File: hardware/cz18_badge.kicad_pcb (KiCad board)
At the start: 2 copper layers, 91.5 x 99.6 mm, 37 parts, among them J1 Dev breakout (opt.), J2 VCC (max 5V), J3 GND, J4 LEDS OUT, SW1 MODE, SW2 SLOT, SW3 LEARN, SW4 PLAY, U1 CHQ1838, U2 NRF24L01 (opt.)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

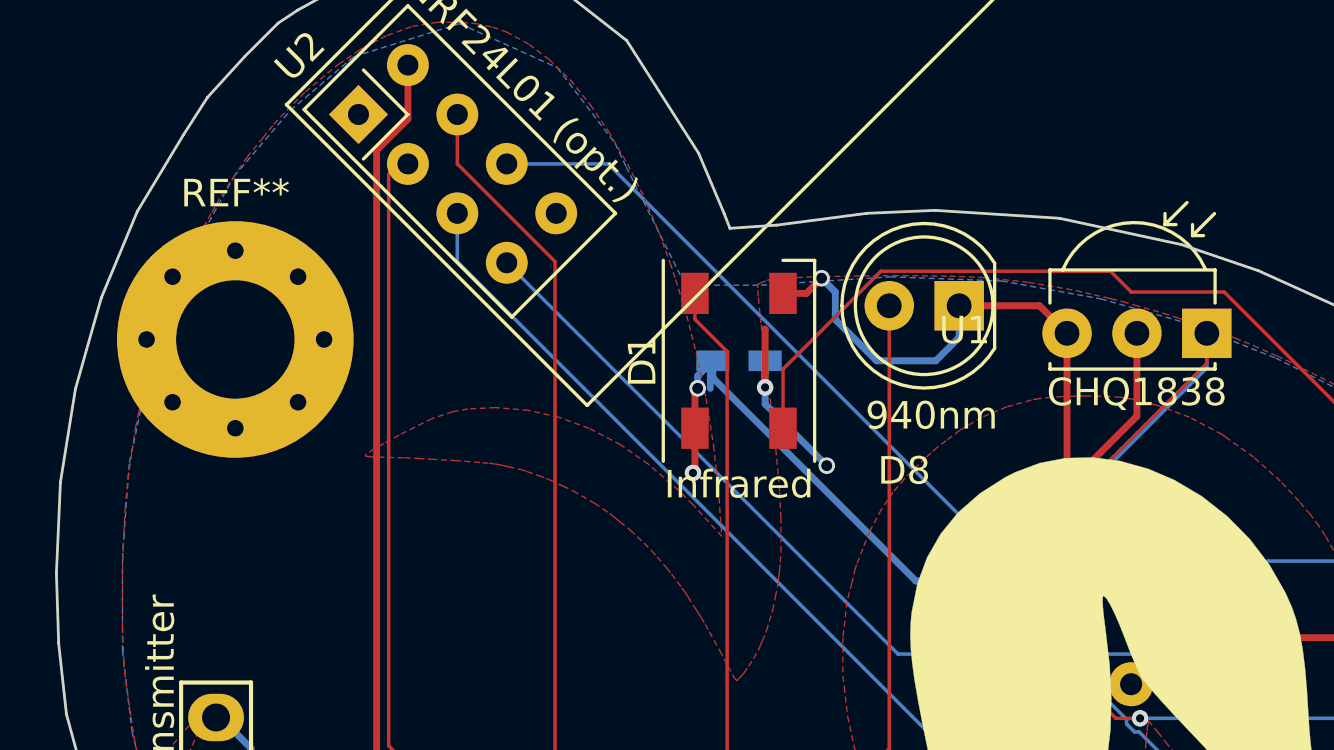
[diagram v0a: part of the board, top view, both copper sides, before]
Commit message: Fixed IR receiver pinout not matching CHQ1838
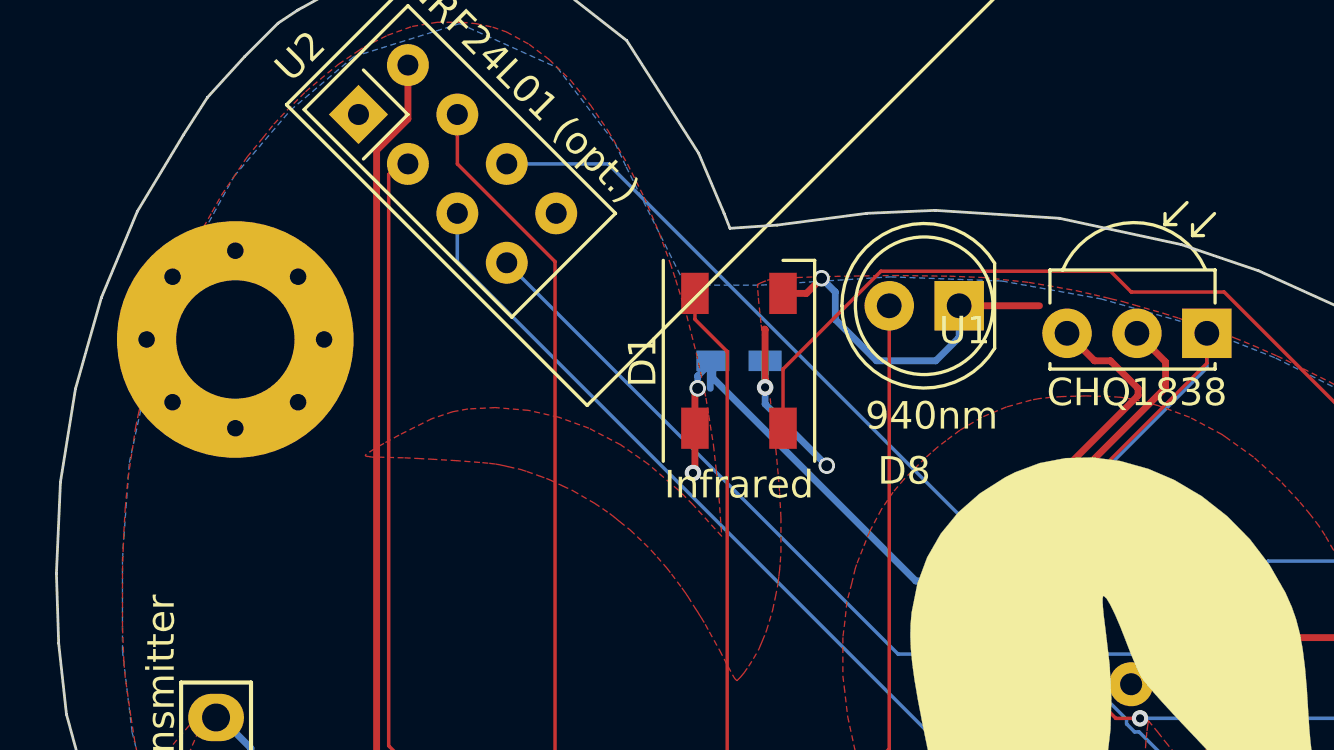
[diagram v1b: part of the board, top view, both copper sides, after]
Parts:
- renumbered REF** to ?
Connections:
- U1 pad 2: VCC -> GND
- U1 pad 3: GND -> VCC
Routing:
- net VCC: track 170.0 -> 171.6 mm
- net GND: track 454.3 -> 455.4 mm
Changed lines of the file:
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@@
     (thickness 1.6)
     (drawings 430)
-    (tracks 1076)
+    (tracks 1083)
     (zones 0)
     (modules 37)
@@
     (mod_text_size 1 1)
     (mod_text_width 0.15)
-    (pad_size 2 2)
-    (pad_drill 1.1)
+    (pad_size 1.8 1.8)
+    (pad_drill 0.9)
     (pad_to_mask_clearance 0.2)
     (aux_axis_origin 86 48)
@@
       (net 25 D7))
     (pad 2 thru_hole circle (at 2.54 0 180) (size 1.8 1.8) (drill 0.9) (layers *.Cu *.Mask)
-      (net 3 VCC))
-    (pad 3 thru_hole circle (at 5.08 0 180) (size 1.8 1.8) (drill 0.9) (layers *.Cu *.Mask)
       (net 15 GND))
+    (pad 3 thru_hole circle (at 5.08 0 180) (size 1.8 1.8) (drill 0.9) (layers *.Cu *.Mask)
+      (net 3 VCC))
   )
   (module RF_Modules:nRF24L01_Breakout (layer F.Cu)
@@
     (tags "mounting hole 4.3mm m4")
     (attr virtual)
-    (fp_text reference REF** (at 0 -5.3) (layer F.SilkS)
+    (fp_text reference "" (at 0 -5.3) (layer F.SilkS)
       (effects (font (size 1 1) (thickness 0.15)))
     )
@@
   (segment (start 119.5792 113.0147) (end 144.1434 113.0147) (width 0.127) (layer B.Cu) (net 2))
   (segment (start 119.5792 113.0146) (end 119.5792 113.0147) (width 0.127) (layer B.Cu) (net 2))
+  (segment (start 118.5 71) (end 120.824999 68.675001) (width 0.25) (layer F.Cu) (net 3))
+  (segment (start 120.824999 67.675999) (end 121.175999 67.324999) (width 0.25) (layer F.Cu) (net 3))
+  (segment (start 122.438535 67.324999) (end 125.5 64.263534) (width 0.25) (layer F.Cu) (net 3))
+  (segment (start 120.824999 68.675001) (end 120.824999 67.675999) (width 0.25) (layer F.Cu) (net 3))
+  (segment (start 123.92 63) (end 122.92 62) (width 0.25) (layer F.Cu) (net 3))
+  (segment (start 121.175999 67.324999) (end 122.438535 67.324999) (width 0.25) (layer F.Cu) (net 3))
+  (segment (start 125.5 64.263534) (end 125.5 64) (width 0.25) (layer F.Cu) (net 3))
+  (segment (start 125.5 64) (end 124.5 63) (width 0.25) (layer F.Cu) (net 3))
+  (segment (start 124.5 63) (end 123.92 63) (width 0.25) (layer F.Cu) (net 3))
   (segment (start 139.5 119.75) (end 139.5 119.843502) (width 0.25) (layer B.Cu) (net 3))
   (segment (start 139.5 119.843502) (end 140.328249 120.671751) (width 0.25) (layer B.Cu) (net 3))
@@
   (segment (start 117.425 71) (end 110.05 63.625) (width 0.25) (layer B.Cu) (net 3))
   (segment (start 110.05 63.625) (end 110.05 63) (width 0.25) (layer B.Cu) (net 3))
-  (segment (start 125.46 65.010654) (end 119.470654 71) (width 0.25) (layer F.Cu) (net 3))
-  (segment (start 119.470654 71) (end 118.5 71) (width 0.25) (layer F.Cu) (net 3))
   (via (at 118.5 71) (size 0.6) (drill 0.4) (layers F.Cu B.Cu) (net 3))
-  (segment (start 125.46 62) (end 125.46 65.010654) (width 0.25) (layer F.Cu) (net 3))
   (segment (start 159.35 99.15) (end 158 100.5) (width 0.25) (layer F.Cu) (net 3))
   (segment (start 159.35 97.849758) (end 159.403173 97.796585) (width 0.25) (layer F.Cu) (net 3))
@@
   (segment (start 169.3503 114.9566) (end 169.5442 116.0564) (width 0.127) (layer B.Cu) (net 14))
   (segment (start 132.4329 89.1197) (end 131.7323 88.419) (width 0.127) (layer B.Cu) (net 14))
+  (segment (start 121.5 68) (end 122.470654 68) (width 0.25) (layer F.Cu) (net 15))
+  (segment (start 122.470654 68) (end 126.5 63.970654) (width 0.25) (layer F.Cu) (net 15))
+  (segment (start 126.5 63.970654) (end 126.5 63.04) (width 0.25) (layer F.Cu) (net 15))
+  (segment (start 126.5 63.04) (end 125.46 62) (width 0.25) (layer F.Cu) (net 15))
   (segment (start 159.20559 96.6) (end 157.4 96.6) (width 0.25) (layer F.Cu) (net 15))
   (segment (start 160.6596 99) (end 160.6596 98.05401) (width 0.25) (layer F.Cu) (net 15))
@@
   (via (at 114 60) (size 0.6) (drill 0.4) (layers F.Cu B.Cu) (net 15))
   (segment (start 119 61) (end 121.92 61) (width 0.25) (layer F.Cu) (net 15))
-  (segment (start 121.92 61) (end 122.92 62) (width 0.25) (layer F.Cu) (net 15))
   (segment (start 111.95 63) (end 111.95 64.570404) (width 0.25) (layer B.Cu) (net 15))
   (segment (start 111.95 64.570404) (end 114.189798 66.810202) (width 0.25) (layer B.Cu) (net 15))
@@
   (segment (start 128.24299 70.24299) (end 128.5 70.5) (width 0.25) (layer B.Cu) (net 15))
   (via (at 128.5 70.5) (size 0.6) (drill 0.4) (layers F.Cu B.Cu) (net 15))
-  (segment (start 122.92 62) (end 122.92 66.58) (width 0.25) (layer F.Cu) (net 15))
-  (segment (start 122.92 66.58) (end 121.5 68) (width 0.25) (layer F.Cu) (net 15))
   (via (at 121.5 68) (size 0.6) (drill 0.4) (layers F.Cu B.Cu) (net 15))
   (segment (start 112.719743 106.280257) (end 110.5909 108.4091) (width 0.25) (layer F.Cu) (net 15))
